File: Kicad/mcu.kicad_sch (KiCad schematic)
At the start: 23 parts, among them J10 Conn_01x03_Pin, J2 USB_B_Micro, J4 Conn_02x03_Top_Bottom, U4 STM32G431CBT6

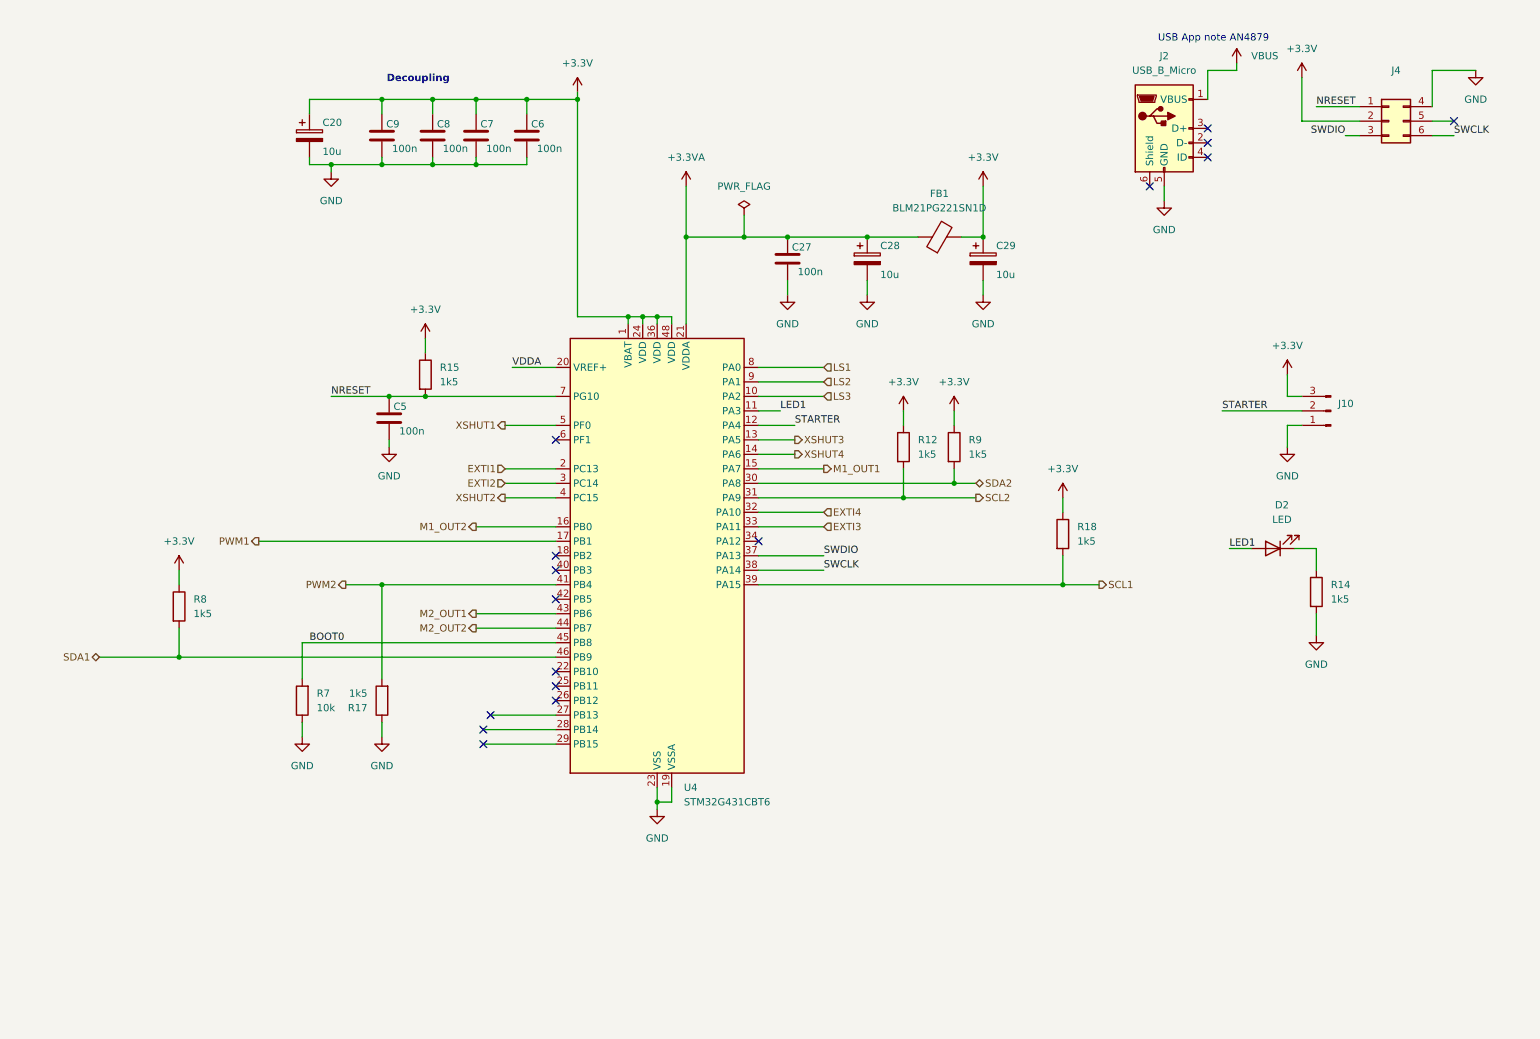
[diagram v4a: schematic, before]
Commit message: kicad schemas documentation
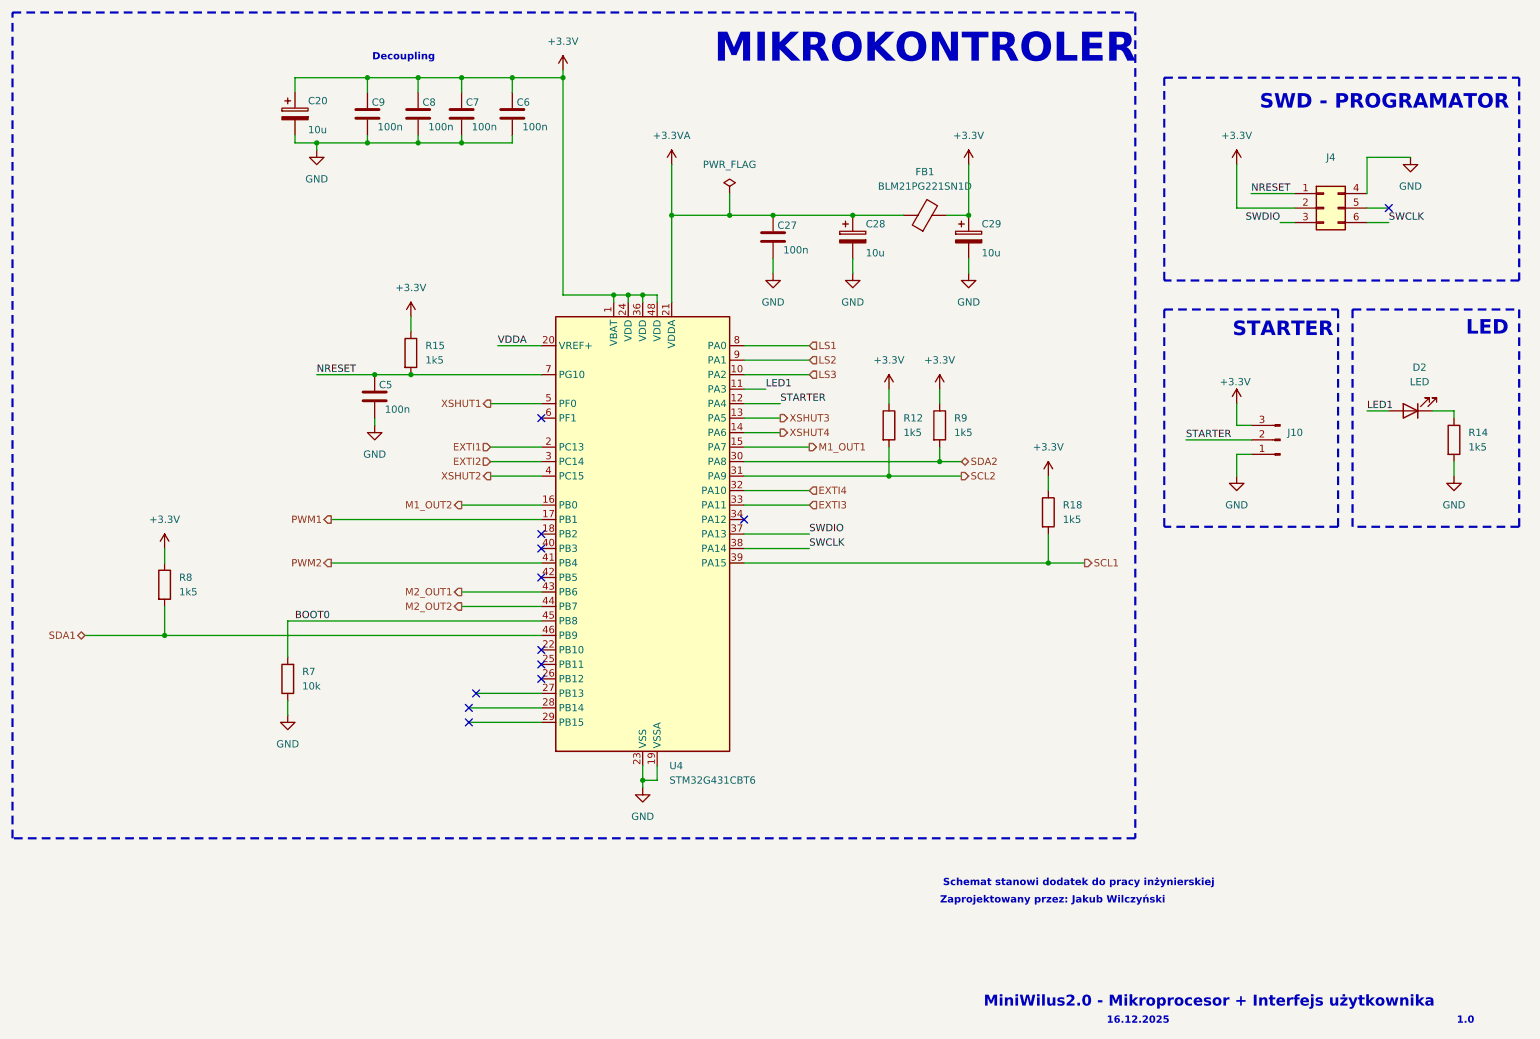
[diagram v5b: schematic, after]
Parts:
- removed J2: USB_B_Micro, Connector_USB:USB_Micro-B_Amphenol_10118194-0001LF_Horizontal, symbol Connector:USB_B_Micro
- removed R17: 1k5, Resistor_SMD:R_0805_2012Metric_Pad1.20x1.40mm_HandSolder, symbol Device:R
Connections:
- no-connect marks 16 -> 12
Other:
- note added: "1.0"
- note added: "16.12.2025"
- note added: "LED"
- note added: "MIKROKONTROLER"
- note added: "MiniWilus2.0 - Mikroprocesor + Interfejs użytkownika"
- note added: "STARTER"
- note added: "SWD - PROGRAMATOR"
- note added: "Schemat stanowi dodatek do pracy inżynierskiej"
- note added: "Zaprojektowany przez: Jakub Wilczyński"
- note removed: "USB App note AN4879"
- moved on the sheet: C20, C27, C28, C29, C5, C6, C7, C8, C9, D2, FB1, J10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
